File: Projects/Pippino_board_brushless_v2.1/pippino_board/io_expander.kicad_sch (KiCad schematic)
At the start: 4 parts, among them J9 IO, U4 MCP23017

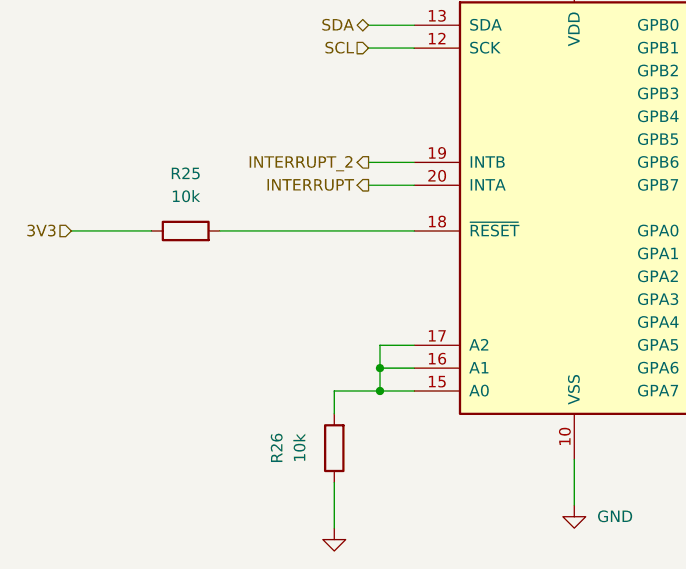
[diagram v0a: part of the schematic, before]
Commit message: moved to ubu 22, updated pippino v2.1
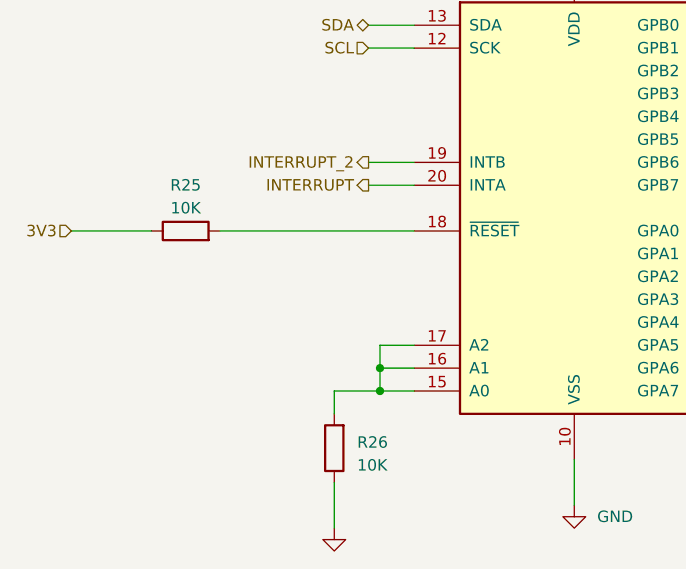
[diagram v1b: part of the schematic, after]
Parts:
- R25, R26: value 10k -> 10K
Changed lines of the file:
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@@
   (symbol (lib_id "Device:R") (at 114.3 72.39 90) (unit 1)
     (in_bom yes) (on_board yes) (dnp no) (fields_autoplaced)
-    (property "Reference" "R25" (at 114.3 66.04 90)
+    (property "Reference" "R25" (at 114.3 67.31 90)
       (effects (font (size 1.27 1.27)))
     )
-    (property "Value" "10k" (at 114.3 68.58 90)
+    (property "Value" "10K" (at 114.3 69.85 90)
       (effects (font (size 1.27 1.27)))
     )
@@
   (symbol (lib_id "Device:R") (at 130.81 96.52 180) (unit 1)
     (in_bom yes) (on_board yes) (dnp no) (fields_autoplaced)
-    (property "Reference" "R26" (at 124.46 96.52 90)
-      (effects (font (size 1.27 1.27)))
+    (property "Reference" "R26" (at 133.35 95.885 0)
+      (effects (font (size 1.27 1.27)) (justify right))
     )
-    (property "Value" "10k" (at 127 96.52 90)
-      (effects (font (size 1.27 1.27)))
+    (property "Value" "10K" (at 133.35 98.425 0)
+      (effects (font (size 1.27 1.27)) (justify right))
     )
     (property "Footprint" "Resistor_SMD:R_1206_3216Metric" (at 132.588 96.52 90)
